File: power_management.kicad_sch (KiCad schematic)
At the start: 5 parts, among them J5 Conn_01x03, J6 DOCK_PADS, U1 NPM1304-QEAA-R7

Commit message: Organized components in pcb layout editor
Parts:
- added C10: 10µF, Capacitor_SMD:C_0603_1608Metric, symbol Device:C
- added C11: 0.1µF, Capacitor_SMD:C_0603_1608Metric, symbol Device:C
- added C13: 1µF, Capacitor_SMD:C_0603_1608Metric, symbol Device:C
- J6: footprint 1_I-SYST_inc:Dock_Pads_6Pin -> 1_I_Syst.inc:Dock_Pads_6Pin
- U1: footprint 1_I-SYST_inc:QFN50P500X500X90-33N -> 1_I_Syst.inc:QFN50P500X500X90-33N
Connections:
- net GND: now also C10.2, C11.2, C13.2
- net VBUS: now also C13.1
- net VDD: now also C11.1
- net at U1.20 (VSYS), U1.4 (PVDD): now also C10.1

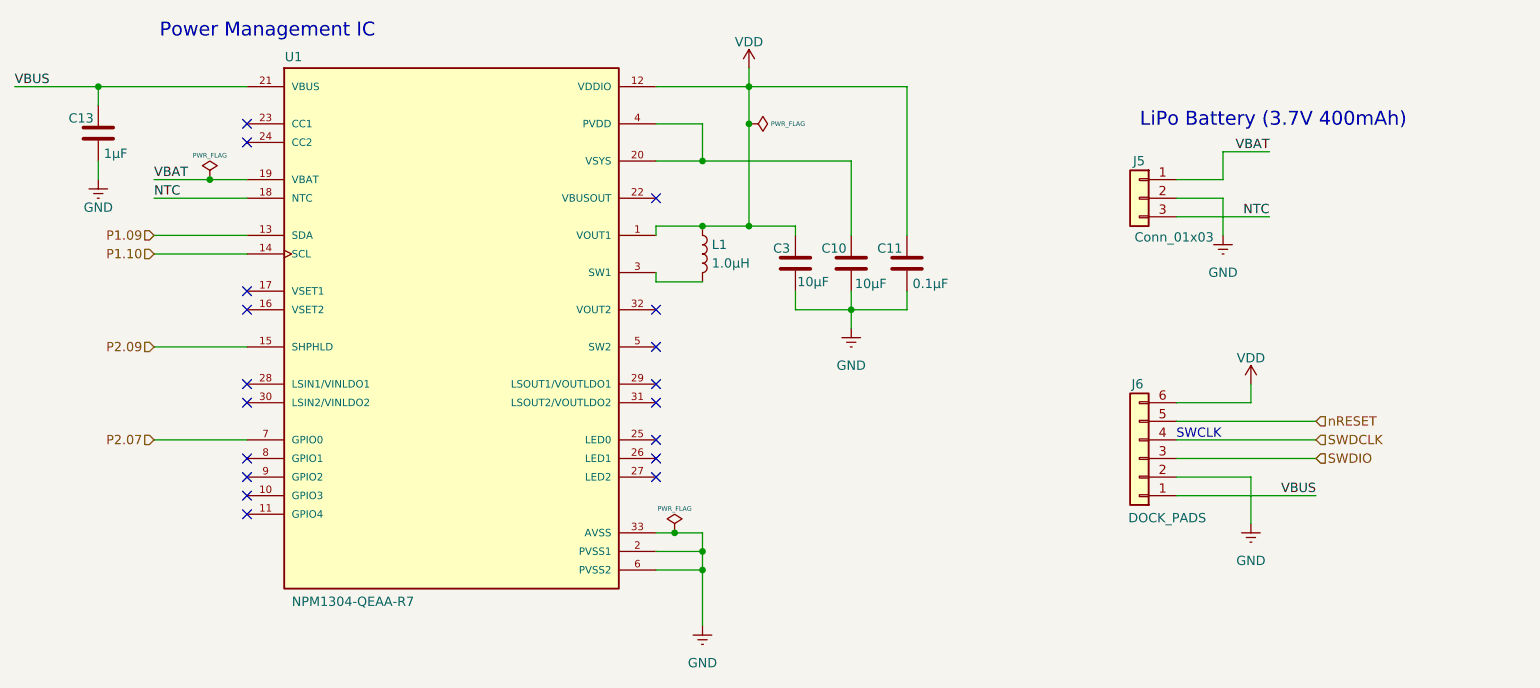
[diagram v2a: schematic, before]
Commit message: PCB traces started
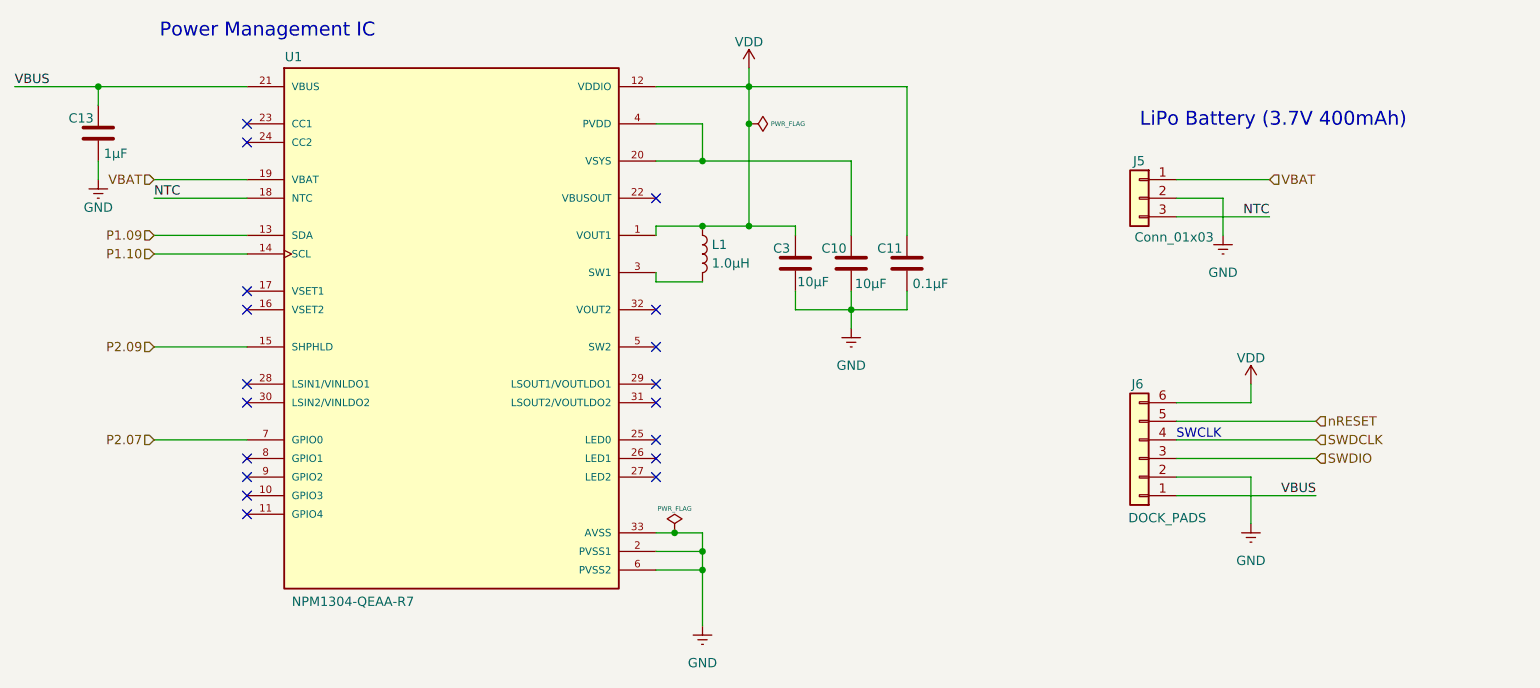
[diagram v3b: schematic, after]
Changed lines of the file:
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@@
-	)
-	(junction
-		(at 60.96 71.12)
-		(diameter 0)
-		(color 0 0 0 0)
 	)
 	(junction
@@
 	(wire
 		(pts
-			(xy 53.34 71.12) (xy 60.96 71.12)
-		)
-		(stroke
-			(width 0)
-			(type default)
-		)
-	)
-	(wire
-		(pts
 			(xy 148.59 88.9) (xy 156.21 88.9)
 		)
@@
 	(wire
 		(pts
-			(xy 199.39 71.12) (xy 199.39 67.31)
-		)
-		(stroke
-			(width 0)
-			(type default)
-		)
-	)
-	(wire
-		(pts
 			(xy 45.72 58.42) (xy 66.04 58.42)
 		)
@@
 	(wire
 		(pts
-			(xy 199.39 67.31) (xy 205.74 67.31)
-		)
-		(stroke
-			(width 0)
-			(type default)
-		)
-	)
-	(wire
-		(pts
 			(xy 148.59 88.9) (xy 148.59 86.36)
 		)
@@
 	(wire
 		(pts
-			(xy 199.39 71.12) (xy 193.04 71.12)
-		)
-		(stroke
-			(width 0)
-			(type default)
-		)
-	)
-	(wire
-		(pts
-			(xy 60.96 71.12) (xy 66.04 71.12)
+			(xy 193.04 71.12) (xy 205.74 71.12)
+		)
+		(stroke
+			(width 0)
+			(type default)
+		)
+	)
+	(wire
+		(pts
+			(xy 53.34 71.12) (xy 66.04 71.12)
 		)
 		(stroke
@@
 		)
 	)
-	(label "VBAT"
-		(at 205.74 67.31 180)
-		(effects
-			(font
-				(size 1.27 1.27)
-			)
-			(justify right bottom)
-		)
-	)
 	(label "VBUS"
 		(at 212.09 114.3 180)
@@
 			)
 			(justify right bottom)
-		)
-	)
-	(label "VBAT"
-		(at 53.34 71.12 0)
-		(effects
-			(font
-				(size 1.27 1.27)
-			)
-			(justify left bottom)
 		)
 	)
@@
 		)
 	)
+	(hierarchical_label "VBAT"
+		(shape input)
+		(at 205.74 71.12 0)
+		(effects
+			(font
+				(size 1.27 1.27)
+			)
+			(justify left)
+		)
+	)
 	(hierarchical_label "P2.07"
 		(shape input)
@@
 			)
 			(justify left)
+		)
+	)
+	(hierarchical_label "VBAT"
+		(shape input)
+		(at 53.34 71.12 180)
+		(effects
+			(font
+				(size 1.27 1.27)
+			)
+			(justify right)
 		)
 	)
@@
 					(unit 1)
 				)
-			)
-		)
-	)
-	(symbol
-		(lib_id "power:PWR_FLAG")
-		(at 60.96 71.12 0)
-		(unit 1)
-		(body_style 1)
-		(exclude_from_sim no)
-		(in_bom yes)
-		(on_board yes)
-		(in_pos_files yes)
-		(dnp no)
-		(property "Reference" "#FLG02"
-			(at 60.96 69.215 0)
-			(hide yes)
-			(show_name no)
-			(do_not_autoplace no)
-			(effects
-				(font
-					(size 1.27 1.27)
-				)
-			)
-		)
-		(property "Value" "PWR_FLAG"
-			(at 60.96 67.818 0)
-			(show_name no)
-			(do_not_autoplace no)
-			(effects
-				(font
-					(size 0.635 0.635)
-				)
-			)
-		)
-		(property "Footprint" ""
-			(at 60.96 71.12 0)
-			(hide yes)
-			(show_name no)
-			(do_not_autoplace no)
-			(effects
-				(font
-					(size 1.27 1.27)
-				)
-			)
-		)
-		(property "Datasheet" ""
-			(at 60.96 71.12 0)
-			(hide yes)
-			(show_name no)
-			(do_not_autoplace no)
-			(effects
-				(font
-					(size 1.27 1.27)
-				)
-			)
-		)
-		(property "Description" "Special symbol for telling ERC where power comes from"
-			(at 60.96 71.12 0)
-			(hide yes)
-			(show_name no)
-			(do_not_autoplace no)
-			(effects
-				(font
-					(size 1.27 1.27)
-				)
-			)
-		)
-		(pin "1"
-		)
-		(instances
-			(project "blystl15_board"
-				(path "/a40d8082-672d-4873-9a41-379b45d6c2c5/a52411fb-3d74-44f3-8a38-1b3fa275b583"
-					(reference "#FLG02")
-					(unit 1)
-				)

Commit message: Full Redesign of the Watch PCB (DRC still not fully passed)
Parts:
- removed U1: NPM1304-QEAA-R7, 1_I_Syst.inc:QFN50P500X500X90-33N, symbol I_Syst_inc:NPM1304-QEAA-R7
- added C15: 10µF, Capacitor_SMD:C_0603_1608Metric, symbol Device:C
- added L2: 1.0µH, Inductor_SMD:L_0805_2012Metric, symbol Device:L
- added U5: NPM1304-QEAA-R7, 1_I_Syst.inc:QFN50P500X500X90-33N, symbol I_Syst_inc:NPM1304-QEAA-R7
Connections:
- net GND: now also C15.2, U5.2 (PVSS1), U5.33 (AVSS), U5.6 (PVSS2)
- net NTC: now also U5.18 (NTC)
- net VBAT: now also U5.19 (VBAT)
- net VBUS: now also U5.21 (VBUS)
- net VDD: now also U5.1 (VOUT1), U5.12 (VDDIO)
- net at C10.1: now also U5.20 (VSYS), U5.4 (PVDD)
- net at L1.2: now also U5.3 (SW1)
- new net: L2.2, U5.5 (SW2)
- new net P1.06: U5.7 (GPIO0)
- new net P1.08: U5.13 (SDA)
- new net P2.01: U5.15 (SHPHLD)
- new net P2.02: U5.14 (SCL)
- new net VDD_3V3: C15.1, L2.1, U5.32 (VOUT2)
- no-connect marks 18 -> 16
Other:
- moved on the sheet: C10, C11, C3, J5, J6
